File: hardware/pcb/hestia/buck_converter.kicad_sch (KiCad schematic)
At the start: 21 parts, among them U1 LM2655MTC-3.3/NOPB

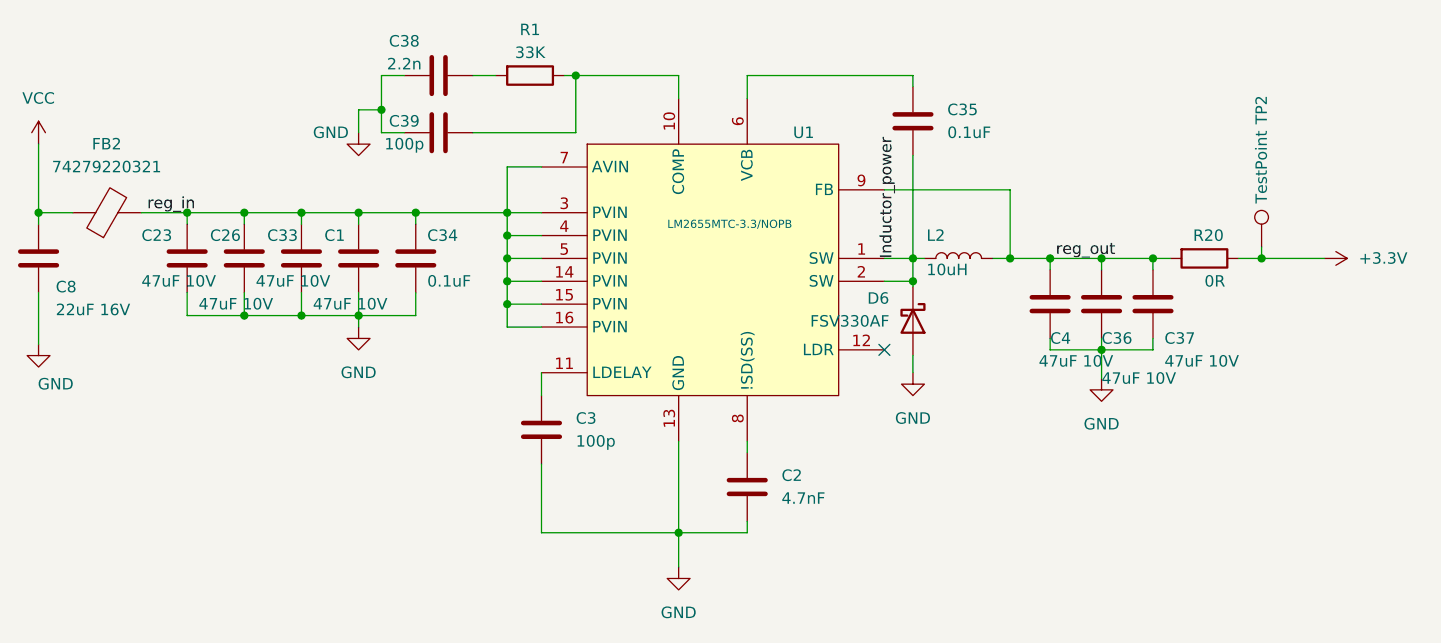
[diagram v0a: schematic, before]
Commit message: added some digikey and mouser part numbers to schematic parts
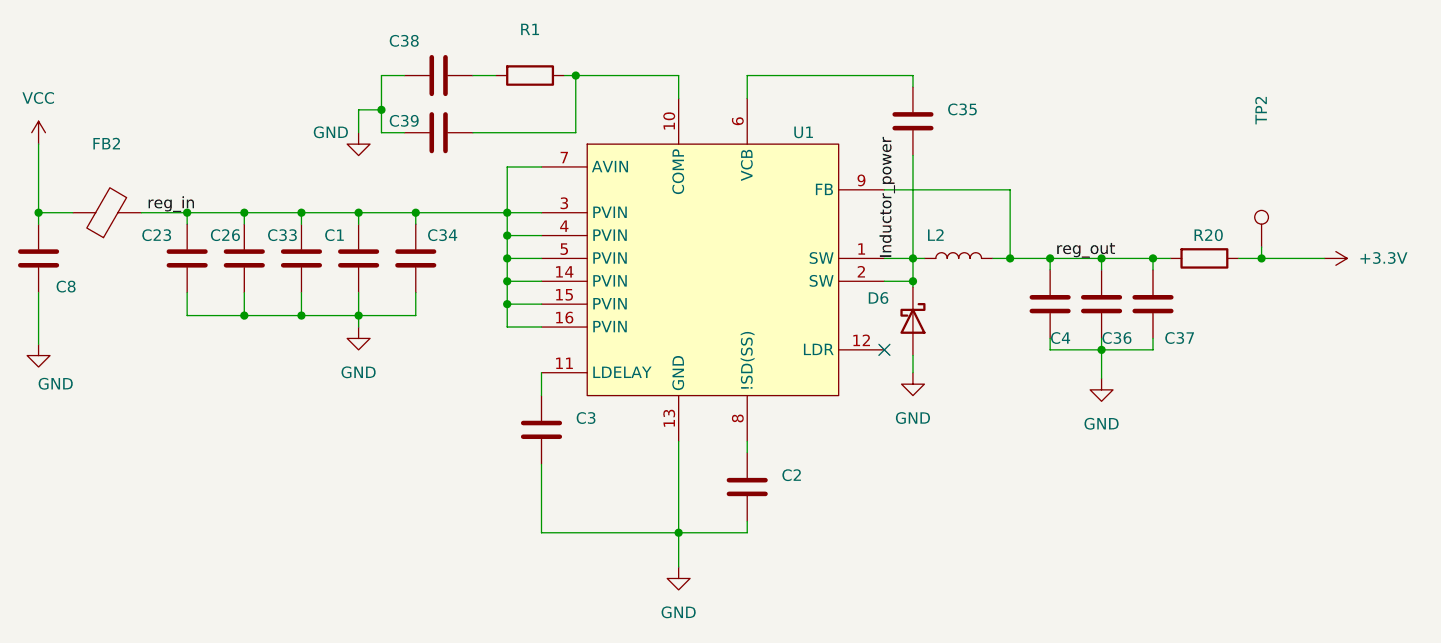
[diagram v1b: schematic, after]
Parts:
- C1, C23, C26, C33, C36, C37, C4: value 47uF 10V -> (none); footprint Capacitor_SMD:C_0805_2012Metric_Pad1.18x1.45mm_HandSolder -> (none); Digikey Part (none) -> 587-5465-1-ND
- C2: value 4.7nF -> (none); footprint Capacitor_SMD:C_0603_1608Metric_Pad1.08x0.95mm_HandSolder -> (none)
- C3, C39: value 100p -> (none); footprint Capacitor_SMD:C_0603_1608Metric_Pad1.08x0.95mm_HandSolder -> (none)
- C34, C35: value 0.1uF -> (none); footprint Capacitor_SMD:C_0603_1608Metric_Pad1.08x0.95mm_HandSolder -> (none)
- C38: value 2.2n -> (none); footprint Capacitor_SMD:C_0603_1608Metric_Pad1.08x0.95mm_HandSolder -> (none)
- C8: value 22uF 16V -> (none); footprint Capacitor_SMD:C_1206_3216Metric -> (none)
- D6: value FSV330AF -> (none); footprint Hestia:DO-214AD (SMAF) -> (none)
- FB2: value 74279220321 -> (none); footprint Resistor_SMD:R_0805_2012Metric_Pad1.20x1.40mm_HandSolder -> (none); Digikey Part (none) -> 732-6125-1-ND
- L2: value 10uH -> (none); footprint Inductor_SMD:L_Coilcraft_LPS5030 -> (none); Digikey Part (none) -> 118-SRP5030C-100MCT-ND
- R1: value 33K -> (none); footprint Resistor_SMD:R_0603_1608Metric_Pad0.98x0.95mm_HandSolder -> (none)
- R20: value 0R -> (none); footprint Resistor_SMD:R_1210_3225Metric_Pad1.30x2.65mm_HandSolder -> (none)
- TP2: value TestPoint -> (none); footprint TestPoint:TestPoint_Pad_2.0x2.0mm -> (none)
- U1: value LM2655MTC-3.3/NOPB -> (none); footprint Package_SO:TSSOP-16_4.4x5mm_P0.65mm -> (none); Digikey Part (none) -> LM2655MTC-3.3/NOPB-ND

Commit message: added more digikey part numbers to schematic
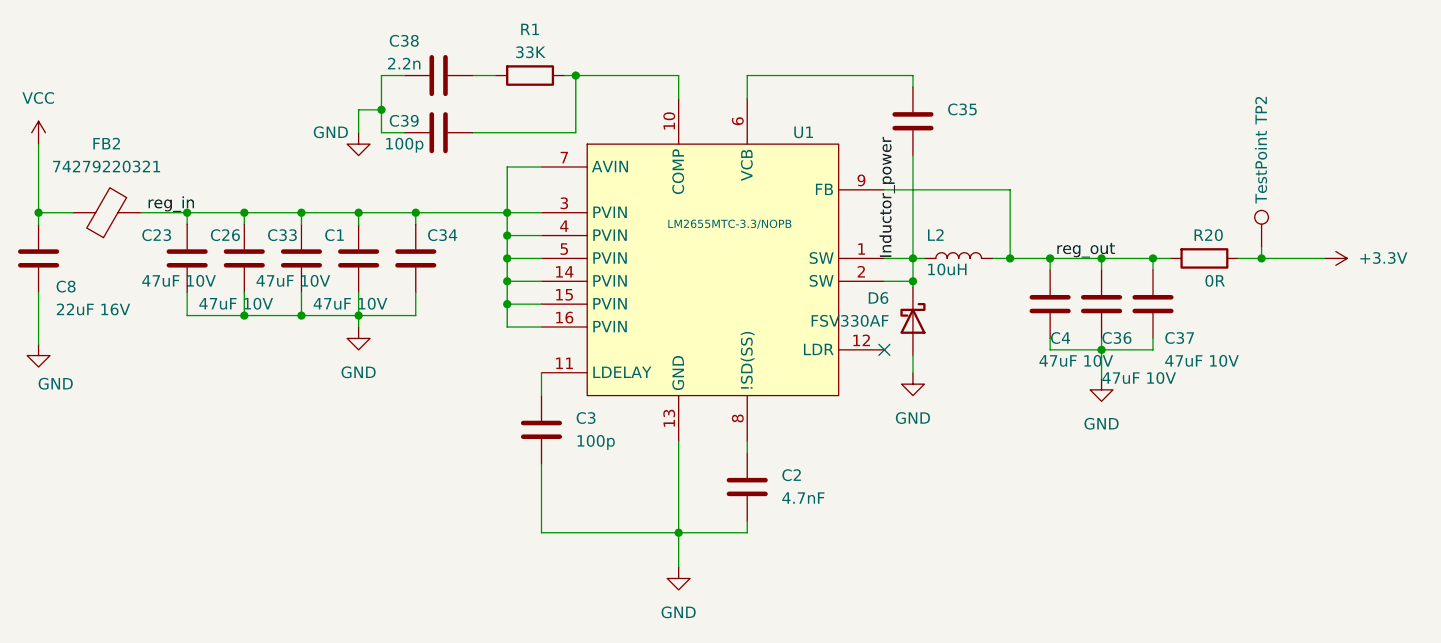
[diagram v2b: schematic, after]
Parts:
- C1, C23, C26, C33, C36, C37, C4: value (none) -> 47uF 10V; footprint (none) -> Capacitor_SMD:C_0805_2012Metric_Pad1.18x1.45mm_HandSolder
- C2: value (none) -> 4.7nF; footprint (none) -> Capacitor_SMD:C_0603_1608Metric_Pad1.08x0.95mm_HandSolder
- C3, C39: value (none) -> 100p; footprint (none) -> Capacitor_SMD:C_0603_1608Metric_Pad1.08x0.95mm_HandSolder
- C34, C35: Digikey Part (none) -> 1276-CL10B104KB8WPNDCT-ND
- C38: value (none) -> 2.2n; footprint (none) -> Capacitor_SMD:C_0603_1608Metric_Pad1.08x0.95mm_HandSolder
- C8: value (none) -> 22uF 16V; footprint (none) -> Capacitor_SMD:C_1206_3216Metric
- D6: value (none) -> FSV330AF; footprint (none) -> Hestia:DO-214AD (SMAF)
- FB2: value (none) -> 74279220321; footprint (none) -> Resistor_SMD:R_0805_2012Metric_Pad1.20x1.40mm_HandSolder
- L2: value (none) -> 10uH; footprint (none) -> Inductor_SMD:L_Coilcraft_LPS5030
- R1: value (none) -> 33K; footprint (none) -> Resistor_SMD:R_0603_1608Metric_Pad0.98x0.95mm_HandSolder
- R20: value (none) -> 0R; footprint (none) -> Resistor_SMD:R_1210_3225Metric_Pad1.30x2.65mm_HandSolder
- TP2: value (none) -> TestPoint; footprint (none) -> TestPoint:TestPoint_Pad_2.0x2.0mm
- U1: value (none) -> LM2655MTC-3.3/NOPB; footprint (none) -> Package_SO:TSSOP-16_4.4x5mm_P0.65mm
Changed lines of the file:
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@@
       (effects (font (size 1.27 1.27)) (justify left))
     )
-    (property "Value" "" (id 1) (at 146.685 86.995 0)
+    (property "Value" "LM2655MTC-3.3/NOPB" (id 1) (at 146.685 86.995 0)
       (effects (font (size 0.9 0.9)) (justify left))
     )
-    (property "Footprint" "" (id 2) (at 155.575 95.885 0)
+    (property "Footprint" "Package_SO:TSSOP-16_4.4x5mm_P0.65mm" (id 2) (at 155.575 95.885 0)
       (effects (font (size 1.27 1.27)) hide)
     )
@@
     (in_bom yes) (on_board yes)
     (property "Reference" "L2" (id 0) (at 176.53 88.265 90))
-    (property "Value" "" (id 1) (at 177.8 92.075 90))
-    (property "Footprint" "" (id 2) (at 179.07 90.805 0)
+    (property "Value" "10uH" (id 1) (at 177.8 92.075 90))
+    (property "Footprint" "Inductor_SMD:L_Coilcraft_LPS5030" (id 2) (at 179.07 90.805 0)
       (effects (font (size 1.27 1.27)) hide)
     )
@@
       (effects (font (size 1.27 1.27)) (justify left))
     )
-    (property "Value" "" (id 1) (at 78.74 96.52 0)
-      (effects (font (size 1.27 1.27)) (justify left))
-    )
-    (property "Footprint" "" (id 2) (at 77.8002 94.615 0)
+    (property "Value" "22uF 16V" (id 1) (at 78.74 96.52 0)
+      (effects (font (size 1.27 1.27)) (justify left))
+    )
+    (property "Footprint" "Capacitor_SMD:C_1206_3216Metric" (id 2) (at 77.8002 94.615 0)
       (effects (font (size 1.27 1.27)) hide)
     )
@@
       (effects (font (size 1.27 1.27)) hide)
     )
+    (property "Digikey Part" "1276-CL10B104KB8WPNDCT-ND" (id 5) (at 118.745 90.805 0)
+      (effects (font (size 1.27 1.27)) hide)
+    )
     (pin "1")
     (pin "2")
@@
     (in_bom yes) (on_board yes)
     (property "Reference" "TP2" (id 0) (at 212.725 74.295 90))
-    (property "Value" "" (id 1) (at 212.725 80.645 90))
-    (property "Footprint" "" (id 2) (at 217.805 89.535 0)
+    (property "Value" "TestPoint" (id 1) (at 212.725 80.645 90))
+    (property "Footprint" "TestPoint:TestPoint_Pad_2.0x2.0mm" (id 2) (at 217.805 89.535 0)
       (effects (font (size 1.27 1.27)) hide)
     )
@@
     (in_bom yes) (on_board yes)
     (property "Reference" "C38" (id 0) (at 117.475 66.675 90))
-    (property "Value" "" (id 1) (at 117.475 69.215 90))
-    (property "Footprint" "" (id 2) (at 117.475 71.4502 0)
+    (property "Value" "2.2n" (id 1) (at 117.475 69.215 90))
+    (property "Footprint" "Capacitor_SMD:C_0603_1608Metric_Pad1.08x0.95mm_HandSolder" (id 2) (at 117.475 71.4502 0)
       (effects (font (size 1.27 1.27)) hide)
     )
@@
       (effects (font (size 1.27 1.27)) (justify left))
     )
-    (property "Value" "" (id 1) (at 94.615 95.885 0)
-      (effects (font (size 1.27 1.27)) (justify left))
-    )
-    (property "Footprint" "" (id 2) (at 100.6602 94.615 0)
+    (property "Value" "47uF 10V" (id 1) (at 94.615 95.885 0)
+      (effects (font (size 1.27 1.27)) (justify left))
+    )
+    (property "Footprint" "Capacitor_SMD:C_0805_2012Metric_Pad1.18x1.45mm_HandSolder" (id 2) (at 100.6602 94.615 0)
       (effects (font (size 1.27 1.27)) hide)
     )
@@
       (effects (font (size 1.27 1.27)) (justify left))
     )
-    (property "Value" "" (id 1) (at 162.56 97.79 90)
-      (effects (font (size 1.27 1.27)) (justify left))
-    )
-    (property "Footprint" "" (id 2) (at 173.99 97.79 0)
+    (property "Value" "FSV330AF" (id 1) (at 162.56 97.79 90)
+      (effects (font (size 1.27 1.27)) (justify left))
+    )
+    (property "Footprint" "Hestia:DO-214AD (SMAF)" (id 2) (at 173.99 97.79 0)
       (effects (font (size 1.27 1.27)) hide)
     )
@@
       (effects (font (size 1.27 1.27)) hide)
     )
+    (property "Digikey Part" "1276-CL10B104KB8WPNDCT-ND" (id 5) (at 173.99 75.565 0)
+      (effects (font (size 1.27 1.27)) hide)
+    )
     (pin "1")
     (pin "2")
@@
       (effects (font (size 1.27 1.27)) (justify left))
     )
-    (property "Value" "" (id 1) (at 100.965 93.345 0)
-      (effects (font (size 1.27 1.27)) (justify left))
-    )
-    (property "Footprint" "" (id 2) (at 107.0102 94.615 0)
+    (property "Value" "47uF 10V" (id 1) (at 100.965 93.345 0)
+      (effects (font (size 1.27 1.27)) (justify left))
+    )
+    (property "Footprint" "Capacitor_SMD:C_0805_2012Metric_Pad1.18x1.45mm_HandSolder" (id 2) (at 107.0102 94.615 0)
       (effects (font (size 1.27 1.27)) hide)
     )
@@
     (in_bom yes) (on_board yes)
     (property "Reference" "R1" (id 0) (at 131.445 65.405 90))
-    (property "Value" "" (id 1) (at 131.445 67.945 90))
-    (property "Footprint" "" (id 2) (at 131.445 68.707 90)
+    (property "Value" "33K" (id 1) (at 131.445 67.945 90))
+    (property "Footprint" "Resistor_SMD:R_0603_1608Metric_Pad0.98x0.95mm_HandSolder" (id 2) (at 131.445 68.707 90)
       (effects (font (size 1.27 1.27)) hide)
     )
@@
       (effects (font (size 1.27 1.27)) (justify left))
     )
-    (property "Value" "" (id 1) (at 206.375 93.345 90)
-      (effects (font (size 1.27 1.27)) (justify left))
-    )
-    (property "Footprint" "" (id 2) (at 206.375 89.027 90)
+    (property "Value" "0R" (id 1) (at 206.375 93.345 90)
+      (effects (font (size 1.27 1.27)) (justify left))
+    )
+    (property "Footprint" "Resistor_SMD:R_1210_3225Metric_Pad1.30x2.65mm_HandSolder" (id 2) (at 206.375 89.027 90)
       (effects (font (size 1.27 1.27)) hide)
     )
@@
       (effects (font (size 1.27 1.27)) (justify left))
     )
-    (property "Value" "" (id 1) (at 194.945 104.14 0)
-      (effects (font (size 1.27 1.27)) (justify left))
-    )
-    (property "Footprint" "" (id 2) (at 195.9102 99.695 0)
+    (property "Value" "47uF 10V" (id 1) (at 194.945 104.14 0)
+      (effects (font (size 1.27 1.27)) (justify left))
+    )
+    (property "Footprint" "Capacitor_SMD:C_0805_2012Metric_Pad1.18x1.45mm_HandSolder" (id 2) (at 195.9102 99.695 0)
       (effects (font (size 1.27 1.27)) hide)
     )
@@
       (effects (font (size 1.27 1.27)) (justify left))
     )
-    (property "Value" "" (id 1) (at 88.265 93.345 0)
-      (effects (font (size 1.27 1.27)) (justify left))
-    )
-    (property "Footprint" "" (id 2) (at 94.3102 94.615 0)
+    (property "Value" "47uF 10V" (id 1) (at 88.265 93.345 0)
+      (effects (font (size 1.27 1.27)) (justify left))
+    )
+    (property "Footprint" "Capacitor_SMD:C_0805_2012Metric_Pad1.18x1.45mm_HandSolder" (id 2) (at 94.3102 94.615 0)
       (effects (font (size 1.27 1.27)) hide)
     )
@@
     (in_bom yes) (on_board yes) (fields_autoplaced)
     (property "Reference" "FB2" (id 0) (at 84.4042 78.105 90))
-    (property "Value" "" (id 1) (at 84.4042 80.645 90))
-    (property "Footprint" "" (id 2) (at 84.455 87.503 90)
+    (property "Value" "74279220321" (id 1) (at 84.4042 80.645 90))
+    (property "Footprint" "Resistor_SMD:R_0805_2012Metric_Pad1.20x1.40mm_HandSolder" (id 2) (at 84.455 87.503 90)
       (effects (font (size 1.27 1.27)) hide)
     )
@@
       (effects (font (size 1.27 1.27)) (justify left))
     )
-    (property "Value" "" (id 1) (at 187.96 102.235 0)
-      (effects (font (size 1.27 1.27)) (justify left))
-    )
-    (property "Footprint" "" (id 2) (at 190.1952 99.695 0)
+    (property "Value" "47uF 10V" (id 1) (at 187.96 102.235 0)
+      (effects (font (size 1.27 1.27)) (justify left))
+    )
+    (property "Footprint" "Capacitor_SMD:C_0805_2012Metric_Pad1.18x1.45mm_HandSolder" (id 2) (at 190.1952 99.695 0)
       (effects (font (size 1.27 1.27)) hide)
     )
@@
       (effects (font (size 1.27 1.27)) (justify left))
     )
-    (property "Value" "" (id 1) (at 201.93 102.235 0)
-      (effects (font (size 1.27 1.27)) (justify left))
-    )
-    (property "Footprint" "" (id 2) (at 201.6252 99.695 0)
+    (property "Value" "47uF 10V" (id 1) (at 201.93 102.235 0)
+      (effects (font (size 1.27 1.27)) (justify left))
+    )
+    (property "Footprint" "Capacitor_SMD:C_0805_2012Metric_Pad1.18x1.45mm_HandSolder" (id 2) (at 201.6252 99.695 0)
       (effects (font (size 1.27 1.27)) hide)
     )
@@
     (in_bom yes) (on_board yes)
     (property "Reference" "C39" (id 0) (at 117.475 75.565 90))
-    (property "Value" "" (id 1) (at 117.475 78.105 90))
-    (property "Footprint" "" (id 2) (at 117.475 77.8002 0)
+    (property "Value" "100p" (id 1) (at 117.475 78.105 90))
+    (property "Footprint" "Capacitor_SMD:C_0603_1608Metric_Pad1.08x0.95mm_HandSolder" (id 2) (at 117.475 77.8002 0)
       (effects (font (size 1.27 1.27)) hide)
     )
@@
       (effects (font (size 1.27 1.27)) (justify left))
     )
-    (property "Value" "" (id 1) (at 159.385 117.4749 0)
-      (effects (font (size 1.27 1.27)) (justify left))
-    )
-    (property "Footprint" "" (id 2) (at 156.5402 120.015 0)
+    (property "Value" "4.7nF" (id 1) (at 159.385 117.4749 0)
+      (effects (font (size 1.27 1.27)) (justify left))
+    )
+    (property "Footprint" "Capacitor_SMD:C_0603_1608Metric_Pad1.08x0.95mm_HandSolder" (id 2) (at 156.5402 120.015 0)
       (effects (font (size 1.27 1.27)) hide)
     )
@@
       (effects (font (size 1.27 1.27)) (justify right))
     )
-    (property "Value" "" (id 1) (at 136.525 111.1249 0)
+    (property "Value" "100p" (id 1) (at 136.525 111.1249 0)
       (effects (font (size 1.27 1.27)) (justify right))
     )
-    (property "Footprint" "" (id 2) (at 131.7498 106.045 0)
+    (property "Footprint" "Capacitor_SMD:C_0603_1608Metric_Pad1.08x0.95mm_HandSolder" (id 2) (at 131.7498 106.045 0)
       (effects (font (size 1.27 1.27)) hide)
     )
@@
       (effects (font (size 1.27 1.27)) (justify left))
     )
-    (property "Value" "" (id 1) (at 107.315 95.885 0)
-      (effects (font (size 1.27 1.27)) (justify left))
-    )
-    (property "Footprint" "" (id 2) (at 113.3602 94.615 0)
-      (effects (font (size 1.27 1.27)) hide)
-    )
+    (property "Value" "47uF 10V" (id 1) (at 107.315 95.885 0)
+      (effects (font (size 1.27 1.27)) (justify left))
+    )
+    (property "Footprint" "Capacitor_SMD:C_0805_2012Metric_Pad1.18x1.45mm_HandSolder" (id 2) (at 113.3602 94.615 0)
+      (effects (font (size 1.27 1.27)) hide)
+    )

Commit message: added more digikey part numbers to schematic
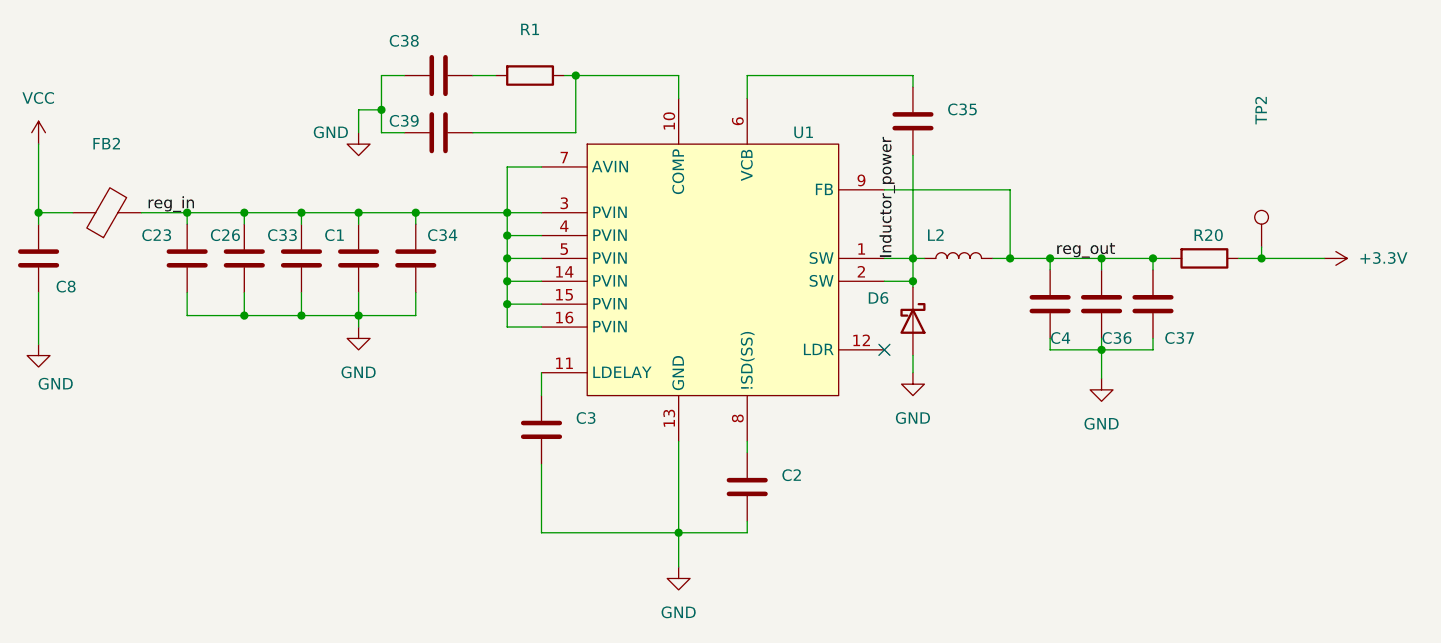
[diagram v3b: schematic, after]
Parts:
- C1, C23, C26, C33, C36, C37, C4: value 47uF 10V -> (none); footprint Capacitor_SMD:C_0805_2012Metric_Pad1.18x1.45mm_HandSolder -> (none)
- C2: value 4.7nF -> (none); footprint Capacitor_SMD:C_0603_1608Metric_Pad1.08x0.95mm_HandSolder -> (none); Digikey Part (none) -> 1276-6532-1-ND
- C3, C39: value 100p -> (none); footprint Capacitor_SMD:C_0603_1608Metric_Pad1.08x0.95mm_HandSolder -> (none)
- C38: value 2.2n -> (none); footprint Capacitor_SMD:C_0603_1608Metric_Pad1.08x0.95mm_HandSolder -> (none); Digikey Part (none) -> 399-6871-1-ND
- C8: value 22uF 16V -> (none); footprint Capacitor_SMD:C_1206_3216Metric -> (none); Digikey Part (none) -> 1276-2728-1-ND
- D6: value FSV330AF -> (none); footprint Hestia:DO-214AD (SMAF) -> (none)
- FB2: value 74279220321 -> (none); footprint Resistor_SMD:R_0805_2012Metric_Pad1.20x1.40mm_HandSolder -> (none)
- L2: value 10uH -> (none); footprint Inductor_SMD:L_Coilcraft_LPS5030 -> (none)
- R1: value 33K -> (none); footprint Resistor_SMD:R_0603_1608Metric_Pad0.98x0.95mm_HandSolder -> (none); Digikey Part (none) -> ERJ-PA3F3302V
- R20: value 0R -> (none); footprint Resistor_SMD:R_1210_3225Metric_Pad1.30x2.65mm_HandSolder -> (none)
- TP2: value TestPoint -> (none); footprint TestPoint:TestPoint_Pad_2.0x2.0mm -> (none)
- U1: value LM2655MTC-3.3/NOPB -> (none); footprint Package_SO:TSSOP-16_4.4x5mm_P0.65mm -> (none)
